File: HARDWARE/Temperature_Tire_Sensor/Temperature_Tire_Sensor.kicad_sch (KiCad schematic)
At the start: 25 parts, among them J1 SWD_01x06, J2 CAN_01x04, SW1 RESET, U1 STM32L4P5RET6, Y1 16MGHz

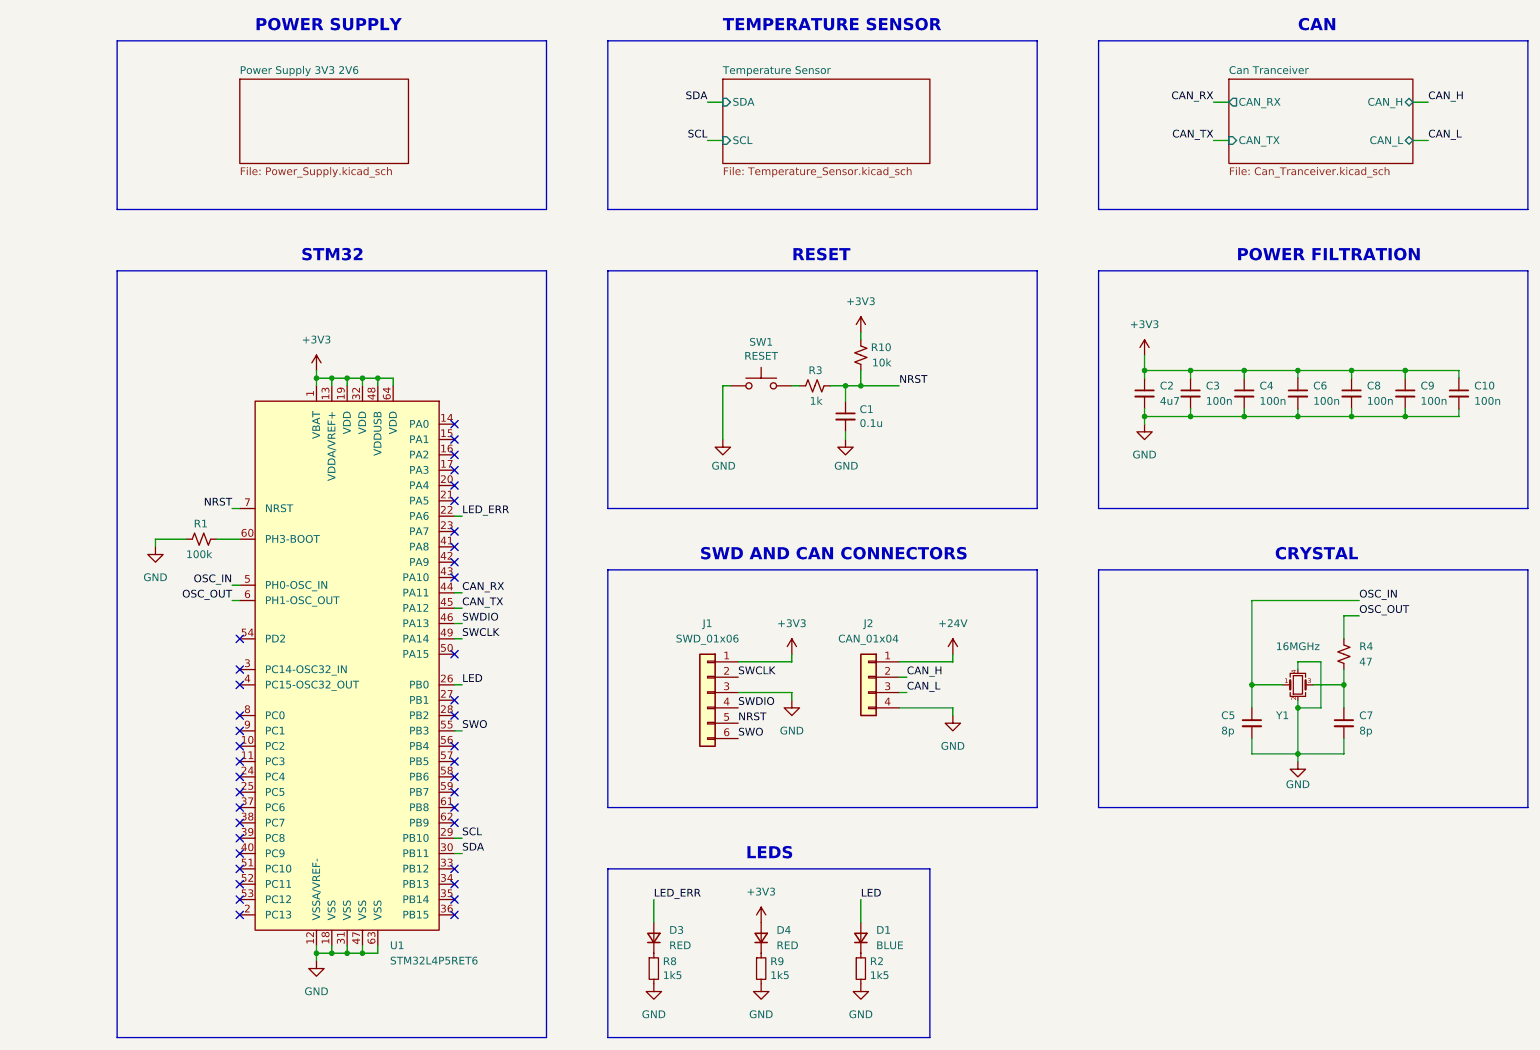
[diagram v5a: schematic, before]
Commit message: Power planes has been added
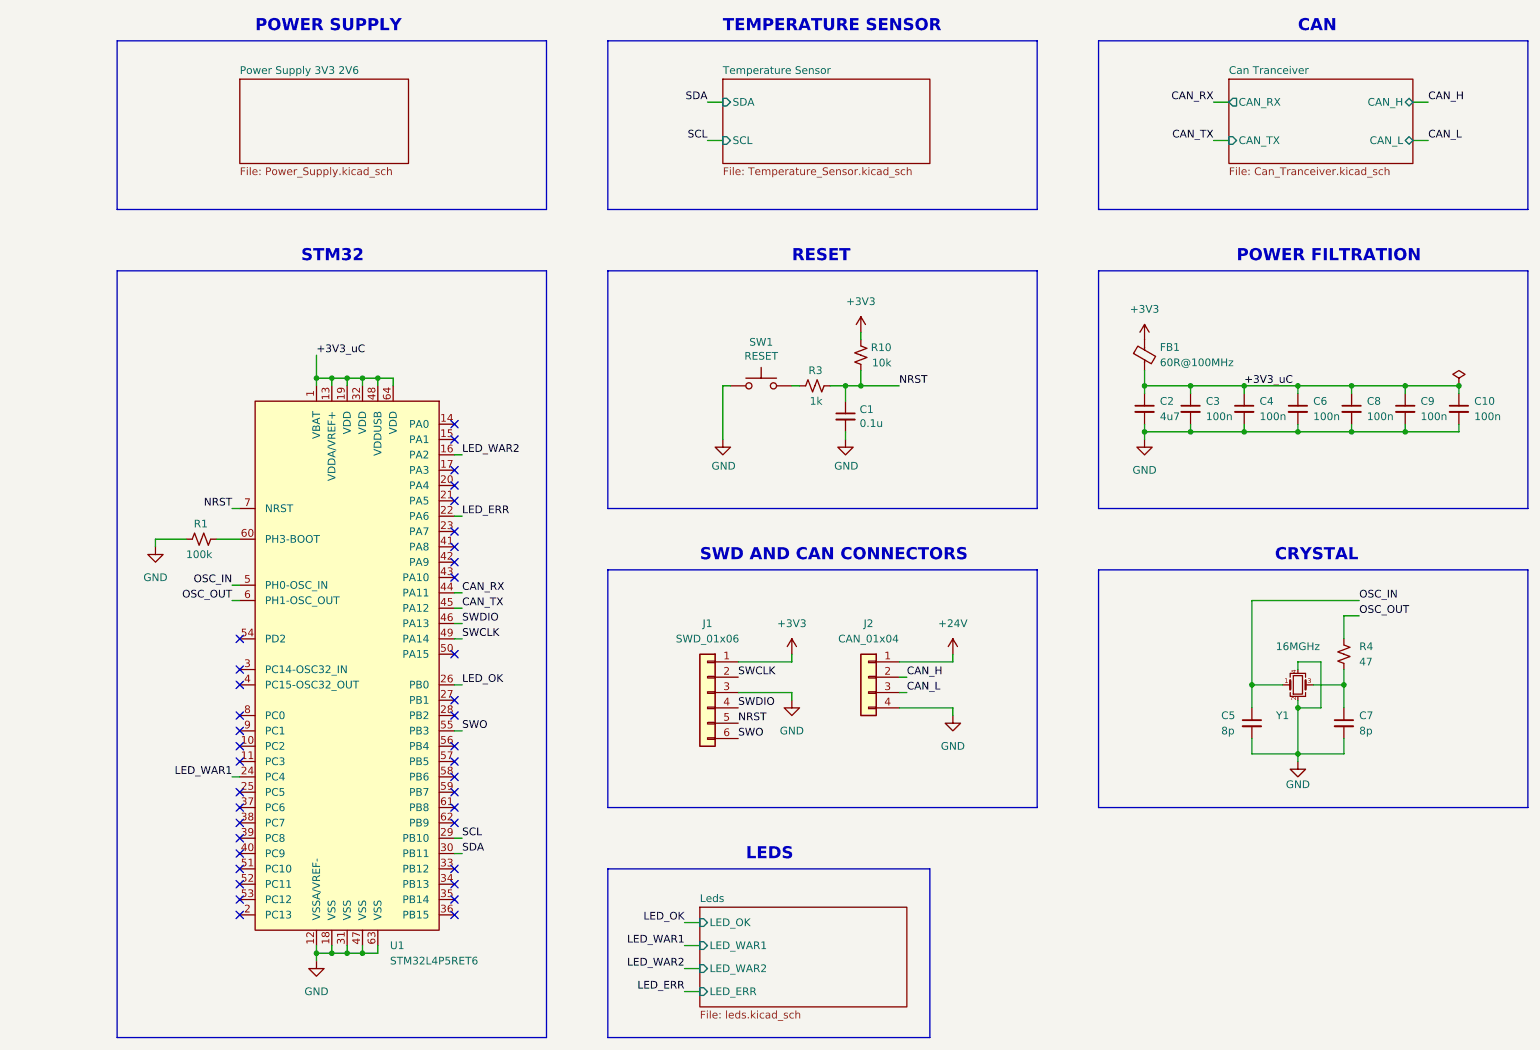
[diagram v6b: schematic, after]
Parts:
- removed D1: BLUE, Diode_SMD:D_0603_1608Metric, symbol Device:D_Small
- removed D3, D4: RED, Diode_SMD:D_0603_1608Metric, symbol Device:D_Small
- removed R2, R8, R9: 1k5, Resistor_SMD:R_0603_1608Metric, symbol SB-Spoko-Bezpieczniki-rescue:R_Small-Device
- added FB1: 60R@100MHz, Inductor_SMD:L_0603_1608Metric, symbol Device:FerriteBead_Small
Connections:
- net +3V3: now also FB1.1; no longer C10.1, C2.1, C3.1, C4.1, C6.1, C8.1, C9.1, U1.1 (VBAT), U1.13 (VDDA/VREF+), U1.19 (VDD), U1.32 (VDD), U1.48 (VDDUSB), U1.64 (VDD)
- net LED_WAR2: now reaches U1.16 (PA2)
- net LED_WAR1: now reaches U1.24 (PC4)
- net LED renamed LED_OK
- new net +3V3_uC: C10.1, C2.1, C3.1, C4.1, C6.1, C8.1, C9.1, FB1.2, U1.1 (VBAT), U1.13 (VDDA/VREF+), U1.19 (VDD), U1.32 (VDD), U1.48 (VDDUSB), U1.64 (VDD)
- no-connect marks 40 -> 38
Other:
- added sheet Leds (leds.kicad_sch)
- moved on the sheet: C10, C2, C3, C4, C6, C8, C9
